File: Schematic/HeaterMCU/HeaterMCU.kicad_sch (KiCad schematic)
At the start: 57 parts, among them J301 To PSU Board, J302 To µTracer, J303 Firmware, Q301 BSS138, Q302 BSS138, SW301 RESET, U301 INA219AIDCNR, U302 Display_IPS_1.3_SPI, U303 ATMEGA328P-AU, U304 TPS54302, Y301 8MHz

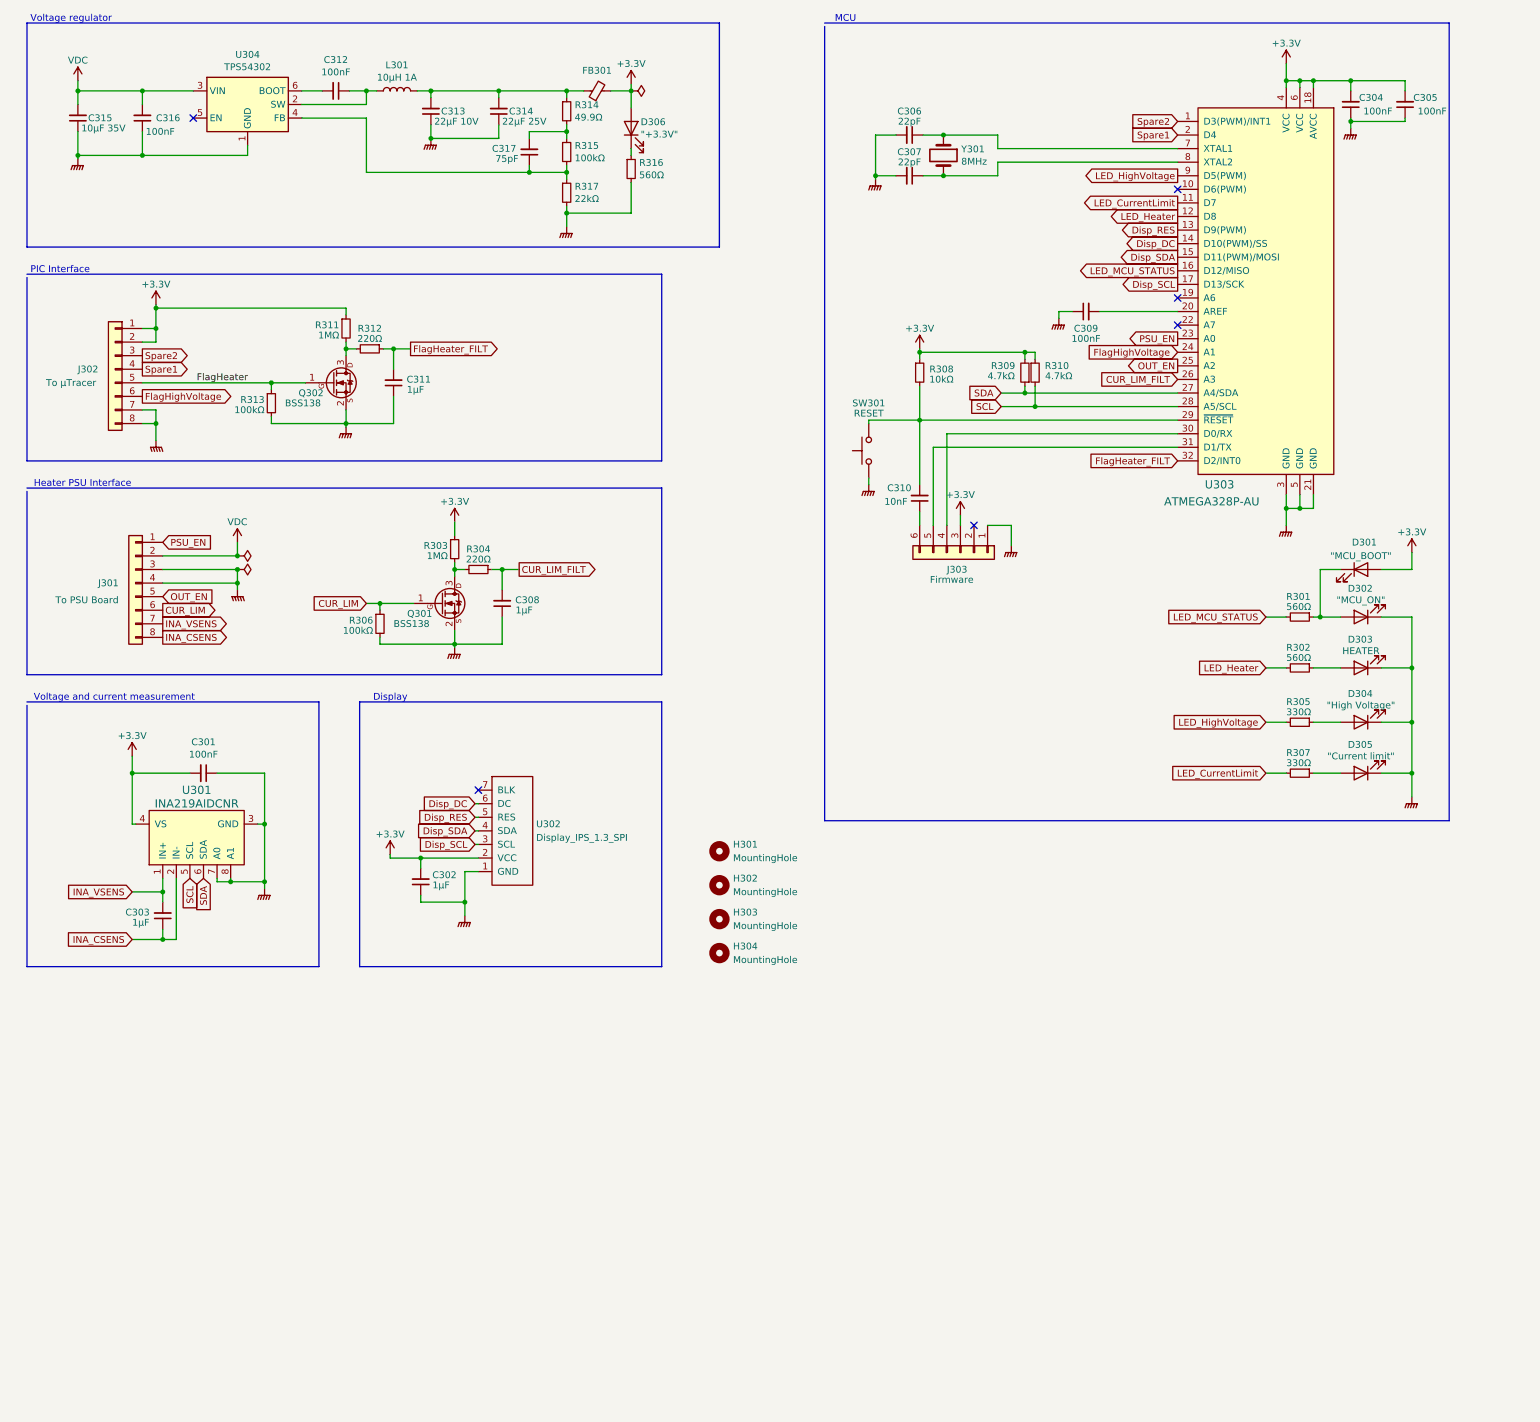
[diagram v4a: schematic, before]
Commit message: Updated pin names
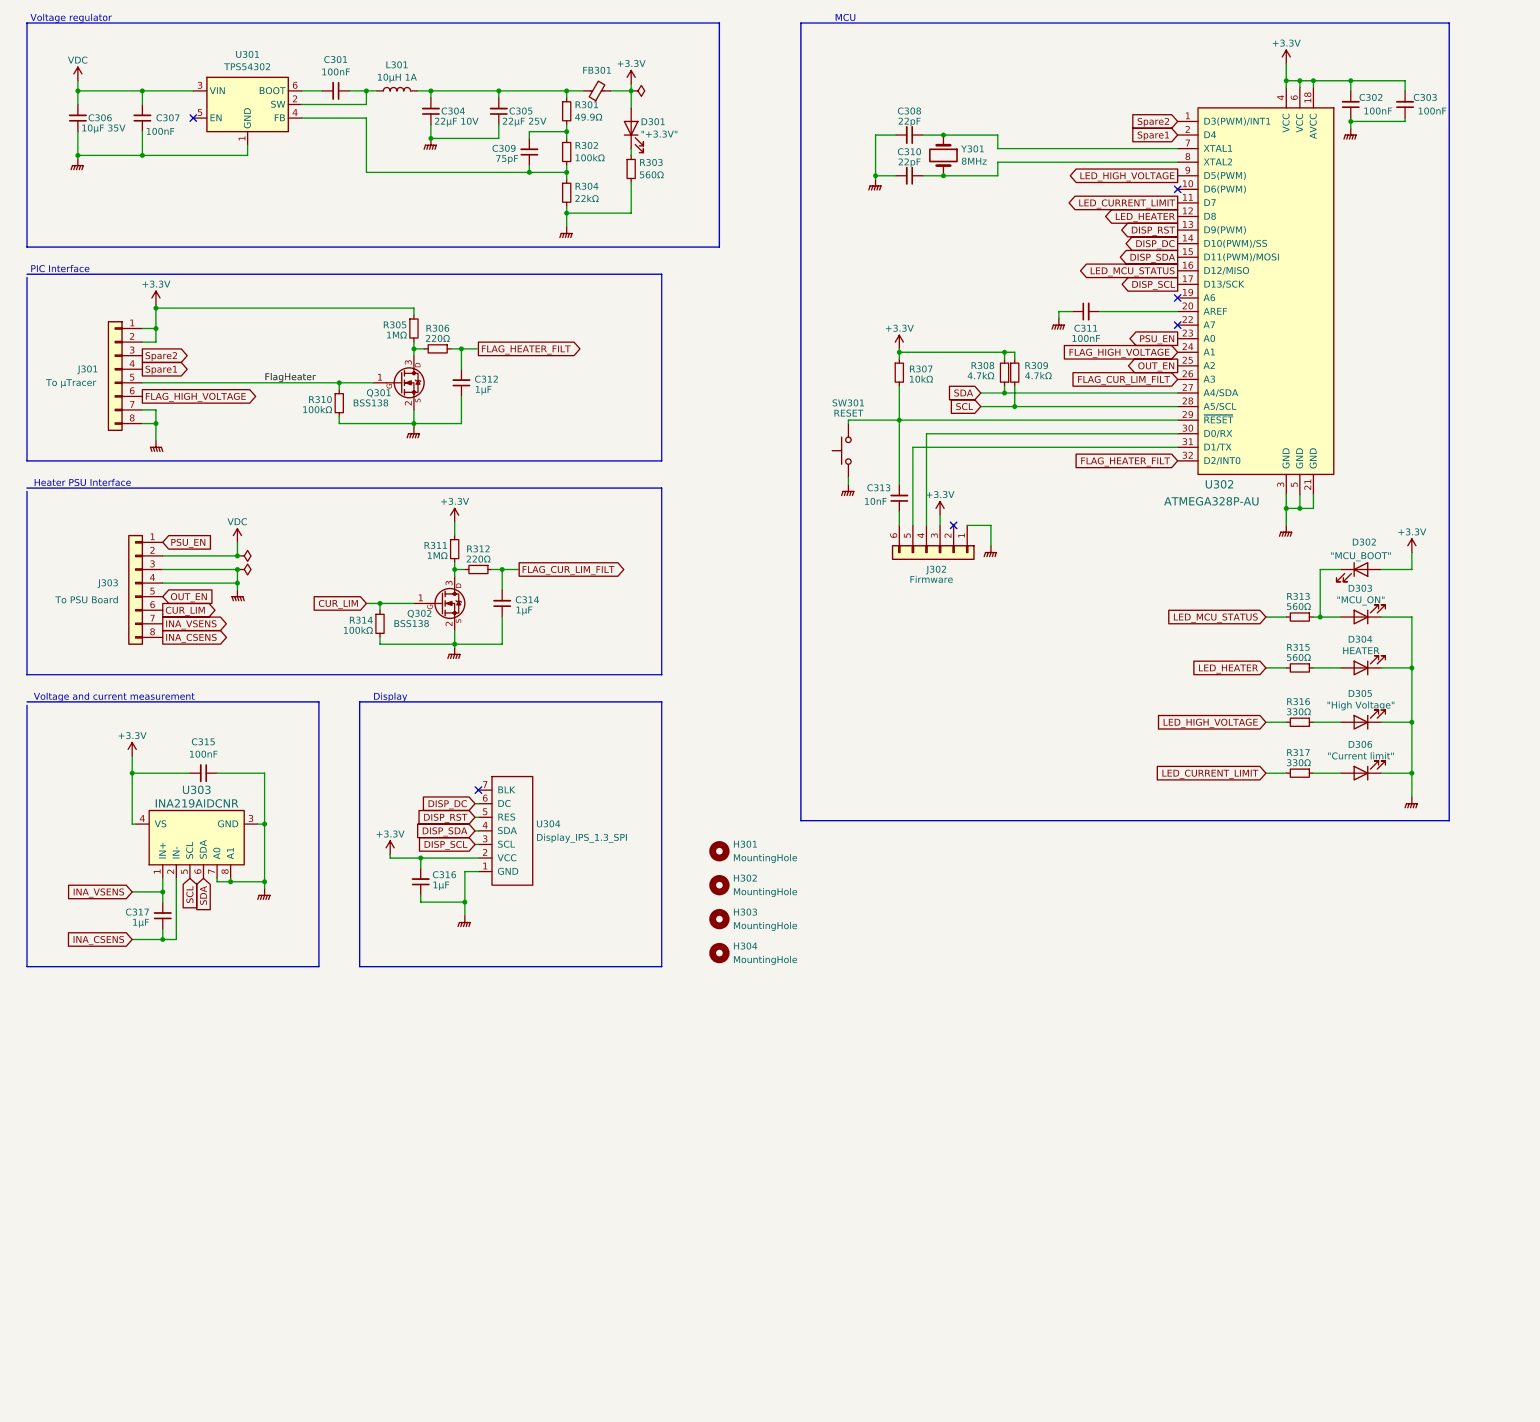
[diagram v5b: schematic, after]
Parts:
- renumbered C312 to C301, C304 to C302, C305 to C303, C313 to C304, C314 to C305, C315 to C306, C316 to C307, C306 to C308, C317 to C309, C307 to C310, C309 to C311, C311 to C312, C310 to C313, C308 to C314, C301 to C315, C302 to C316, C303 to C317, D306 to D301, D301 to D302, D302 to D303, D303 to D304, D304 to D305, D305 to D306, J302 to J301, J303 to J302, J301 to J303, Q302 to Q301, Q301 to Q302, R314 to R301, R315 to R302, R316 to R303, R317 to R304, R311 to R305, R312 to R306, R308 to R307, R309 to R308, R310 to R309, R313 to R310, R303 to R311, R304 to R312, R301 to R313, R306 to R314, R302 to R315, R305 to R316, R307 to R317, U304 to U301, U303 to U302, U301 to U303, U302 to U304
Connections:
- net CUR_LIM_FILT renamed FLAG_CUR_LIM_FILT
- net Disp_DC renamed DISP_DC
- net Disp_RES renamed DISP_RST
- net Disp_SCL renamed DISP_SCL
- net Disp_SDA renamed DISP_SDA
- net FlagHeater_FILT renamed FLAG_HEATER_FILT
- net FlagHighVoltage renamed FLAG_HIGH_VOLTAGE
- net LED_CurrentLimit renamed LED_CURRENT_LIMIT
- net LED_Heater renamed LED_HEATER
- net LED_HighVoltage renamed LED_HIGH_VOLTAGE
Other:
- moved on the sheet: C312, C313, J302, Q301, R305, R306, R307, R308, R309, R310, SW301

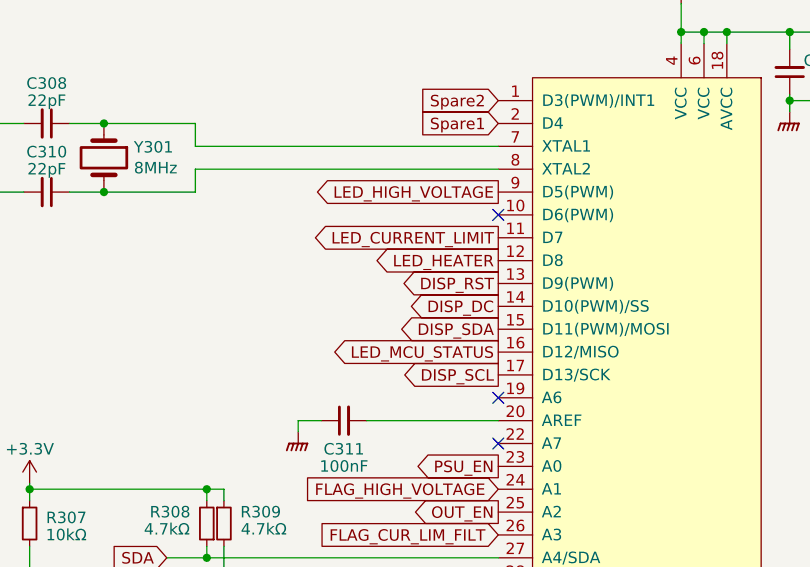
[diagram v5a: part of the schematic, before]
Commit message: Changed pin for MCU status LED
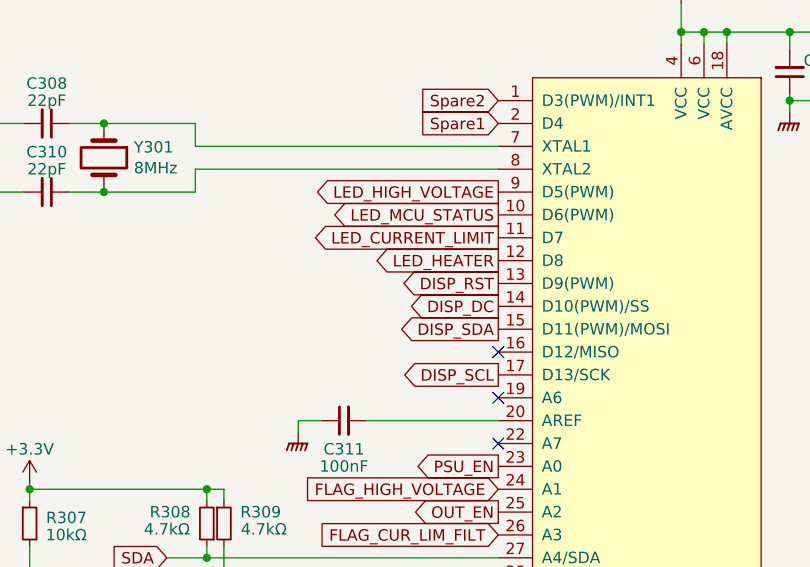
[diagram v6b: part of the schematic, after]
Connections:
- net LED_MCU_STATUS: now also U302.10 (D6(PWM)); no longer U302.16 (D12/MISO)
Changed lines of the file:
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@@
   (no_connect (at 189.23 109.22))
   (no_connect (at 231.14 66.675))
+  (no_connect (at 231.14 61.595))
   (no_connect (at 231.14 71.755))
   (no_connect (at 46.99 33.02))
-  (no_connect (at 231.14 46.355))
   (no_connect (at 100.33 158.75))
   (wire (pts (xy 109.855 43.18) (xy 79.375 43.18))
@@
     )
   )
-  (global_label "LED_MCU_STATUS" (shape output) (at 231.14 61.595 180) (fields_autoplaced)
-    (effects (font (size 1.27 1.27)) (justify right))
-    (property "Intersheet References" "${INTERSHEET_REFS}" (id 0) (at 212.5193 61.5156 0)
-      (effects (font (size 1.27 1.27)) (justify right) hide)
-    )
+  (global_label "LED_MCU_STATUS" (shape output) (at 231.14 46.355 180) (fields_autoplaced)
+    (effects (font (size 1.27 1.27)) (justify right))
+    (property "Intersheet References" "${INTERSHEET_REFS}" (id 0) (at 212.5193 46.2756 0)
+      (effects (font (size 1.27 1.27)) (justify right) hide)
+    )
